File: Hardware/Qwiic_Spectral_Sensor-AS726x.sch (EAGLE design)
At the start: 28 parts, among them J2 Serial Interface, J5 Flash Programming, U1 AS726X, U3 4MB Flash

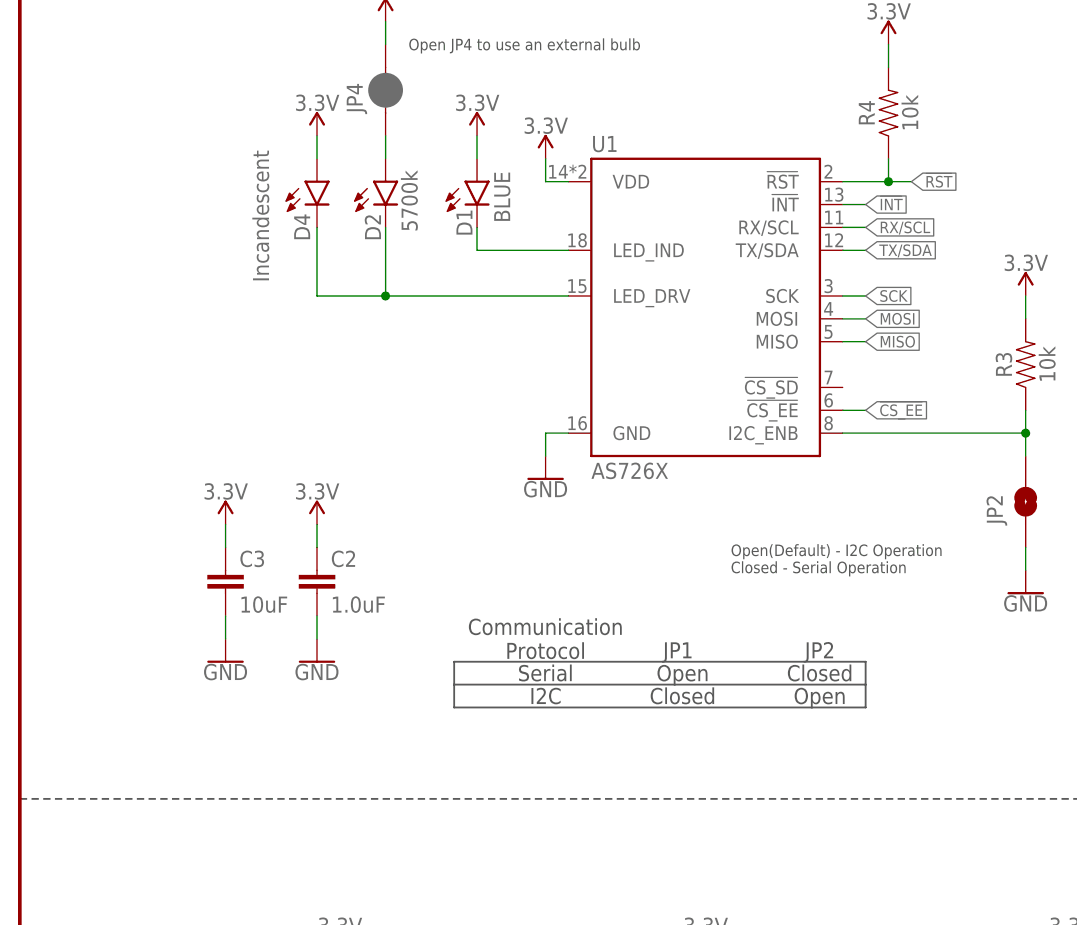
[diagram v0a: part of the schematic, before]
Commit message: Adding AS7263 firmware. Adding I2C address to schematic. Adding LED datasheet.
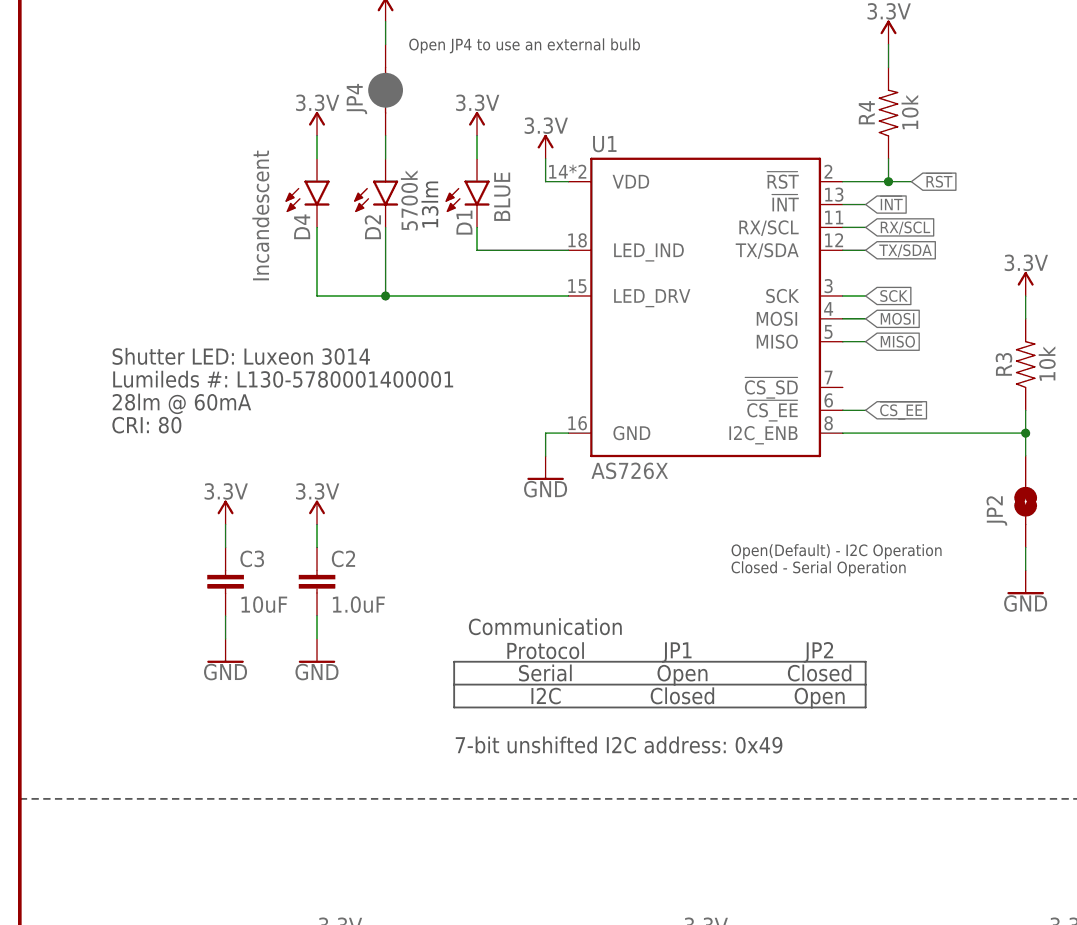
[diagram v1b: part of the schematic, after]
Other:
- note added: "13lm"
- note added: "28lm @ 60mA"
- note added: "7-bit unshifted I2C address: 0x49"
- note added: "CRI: 80"
- note added: "Lumileds #: L130-5780001400001"
- note added: "Shutter LED: Luxeon 3014"
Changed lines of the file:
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@@
 <wire x1="48.26" y1="88.9" x2="48.26" y2="91.44" width="0.2032" layer="97"/>
 <wire x1="48.26" y1="88.9" x2="93.98" y2="88.9" width="0.2032" layer="97"/>
+<text x="46.482" y="139.446" size="1.778" layer="97" rot="R90">13lm</text>
+<text x="10.16" y="121.92" size="1.778" layer="97">Lumileds #: L130-5780001400001</text>
+<text x="10.16" y="124.46" size="1.778" layer="97">Shutter LED: Luxeon 3014</text>
+<text x="10.16" y="119.38" size="1.778" layer="97">28lm @ 60mA</text>
+<text x="10.16" y="116.84" size="1.778" layer="97">CRI: 80</text>
+<text x="48.26" y="81.28" size="1.778" layer="97">7-bit unshifted I2C address: 0x49</text>
 </plain>
 <instances>
